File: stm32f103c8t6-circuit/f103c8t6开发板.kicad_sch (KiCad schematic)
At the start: 0 parts

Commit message: Modify PCH and SCH
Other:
- sheet port renamed Connector
- sheet power renamed Power
- sheet Connector ports: added I2C1_SDA; removed 5V, LED1, LED2, VCC, i2C1_SDA
- sheet MCU ports: added I2C1_SCL, I2C1_SDA; removed LED1, LED2, VCC, i2C1_SCL, i2C1_SDA
- sheet Power ports: added none; removed 5V, VCC

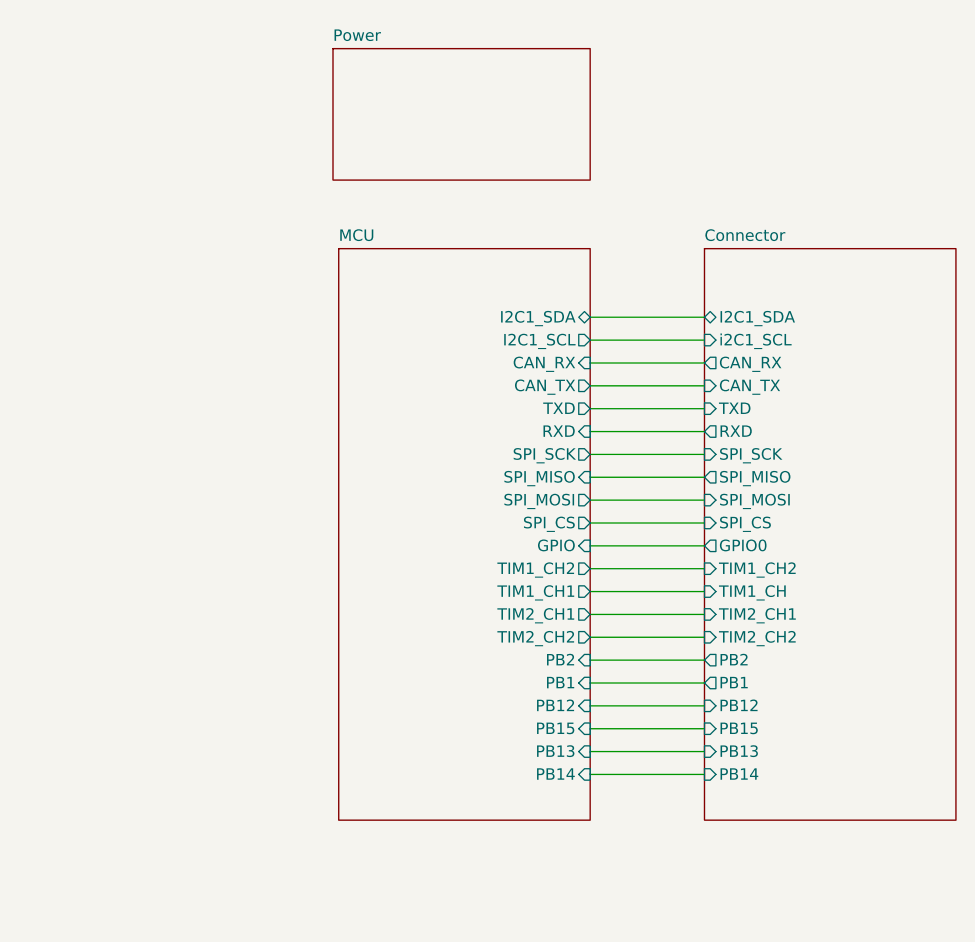
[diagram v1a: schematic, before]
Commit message: Fix some SCH bugs
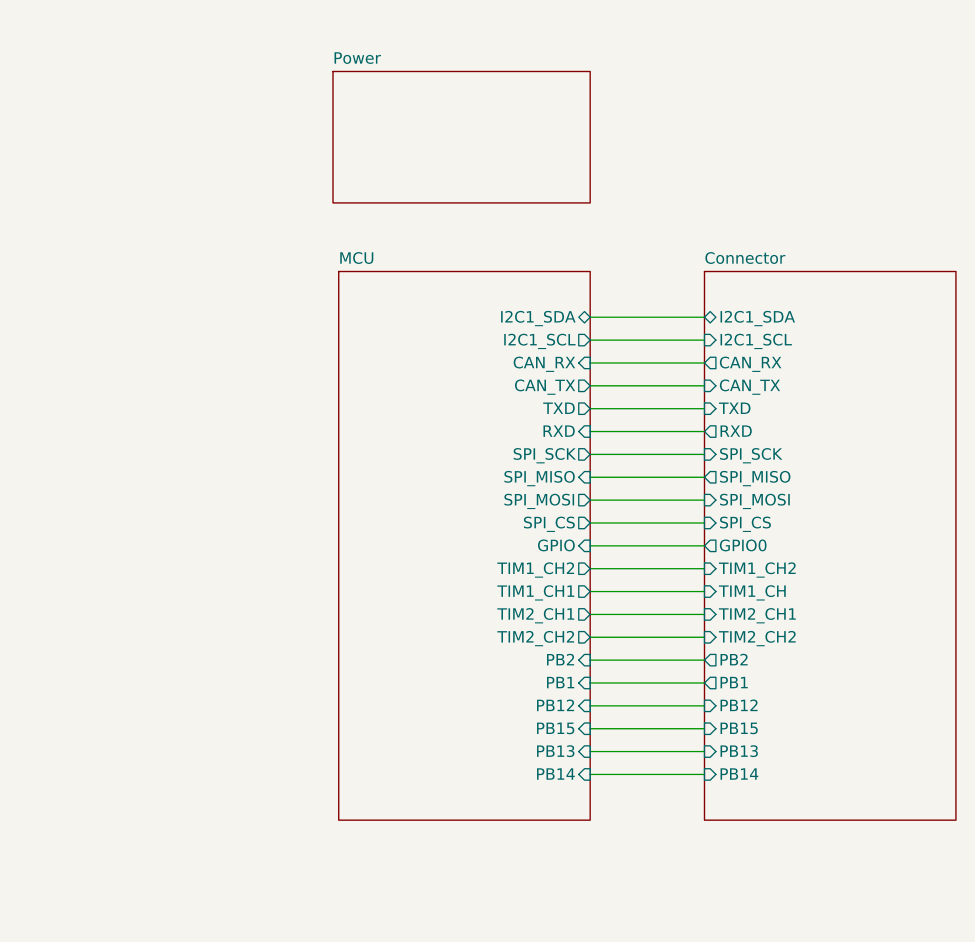
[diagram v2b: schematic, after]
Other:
- sheet Connector ports: added I2C1_SCL; removed i2C1_SCL
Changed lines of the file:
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@@
     (stroke (width 0) (type default))
   )
-  (sheet (at 98.425 51.435) (size 28.575 14.605) (fields_autoplaced)
+  (sheet (at 98.425 53.975) (size 28.575 14.605) (fields_autoplaced)
     (stroke (width 0.1524) (type solid))
     (fill (color 0 0 0 0.0000))
-    (property "Sheetname" "Power" (at 98.425 50.7234 0)
+    (property "Sheetname" "Power" (at 98.425 53.2634 0)
       (effects (font (size 1.27 1.27)) (justify left bottom))
     )
-    (property "Sheetfile" "power.kicad_sch" (at 98.425 66.6246 0)
+    (property "Sheetfile" "power.kicad_sch" (at 98.425 69.1646 0)
       (effects (font (size 1.27 1.27)) (justify left top) hide)
     )
-    (property "字段 2" "" (at 87.63 62.23 0)
+    (property "字段 2" "" (at 87.63 64.77 0)
       (effects (font (size 1.27 1.27)) hide)
     )
-    (property "字段 3" "" (at 87.63 62.23 0)
+    (property "字段 3" "" (at 87.63 64.77 0)
       (effects (font (size 1.27 1.27)) hide)
     )
@@
     )
   )
-  (sheet (at 99.06 73.66) (size 27.94 63.5) (fields_autoplaced)
+  (sheet (at 99.06 76.2) (size 27.94 60.96) (fields_autoplaced)
     (stroke (width 0.1524) (type solid))
     (fill (color 0 0 0 0.0000))
-    (property "Sheetname" "MCU" (at 99.06 72.9484 0)
+    (property "Sheetname" "MCU" (at 99.06 75.4884 0)
       (effects (font (size 1.27 1.27)) (justify left bottom))
     )
@@
       (effects (font (size 1.27 1.27)) (justify left top) hide)
     )
-    (property "字段 2" "" (at 99.06 73.66 0)
+    (property "字段 2" "" (at 99.06 76.2 0)
       (effects (font (size 1.27 1.27)) hide)
     )
@@
     )
   )
-  (sheet (at 139.7 73.66) (size 27.94 63.5) (fields_autoplaced)
+  (sheet (at 139.7 76.2) (size 27.94 60.96) (fields_autoplaced)
     (stroke (width 0.1524) (type solid))
     (fill (color 0 0 0 0.0000))
-    (property "Sheetname" "Connector" (at 139.7 72.9484 0)
+    (property "Sheetname" "Connector" (at 139.7 75.4884 0)
       (effects (font (size 1.27 1.27)) (justify left bottom))
     )
@@
       (effects (font (size 1.27 1.27)) (justify left))
     )
-    (pin "i2C1_SCL" input (at 139.7 83.82 180)
+    (pin "I2C1_SCL" input (at 139.7 83.82 180)
       (effects (font (size 1.27 1.27)) (justify left))
     )
